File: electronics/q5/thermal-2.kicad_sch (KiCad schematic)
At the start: 5 parts, among them U5 Push-pull temperature window

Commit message: Q5 design lock: JLC Basic substitutions, re-verified board, cost estimator
Co-Authored-By: Claude Opus 5.5 <noreply@anthropic.com>
Claude-Session: https://claude.ai/code/session_01UrkzLMrBi6iLPSL5SbMCA7
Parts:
- R14, R15: MPN RC0603FR-07100KL -> 0603WAF1003T5E
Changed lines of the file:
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@@
       (in_bom yes) (on_board yes) (dnp no)
  (property "Reference" "R14" (at 294.64 73.66 0) (effects (font (size 1.524 1.524)))) (property "Value" "100k" (at 294.64 77.46999999999998 0) (effects (font (size 1.524 1.524))))
-      (property "Footprint" "CountFidgetQ5:Resistor_SMD_R_0603_1608Metric" (at 294.64 82.55 0) (effects (font (size 1.27 1.27)) (hide yes))) (property "MPN" "RC0603FR-07100KL" (at 294.64 77.46999999999998 0) (effects (font (size 1.524 1.524)) (hide yes)))
+      (property "Footprint" "CountFidgetQ5:Resistor_SMD_R_0603_1608Metric" (at 294.64 82.55 0) (effects (font (size 1.27 1.27)) (hide yes))) (property "MPN" "0603WAF1003T5E" (at 294.64 77.46999999999998 0) (effects (font (size 1.524 1.524)) (hide yes)))
       (property "Description" "Local upper charge-enable gate pulldown; keep connected close to Q3 gate" (at 294.64 82.55 0) (effects (font (size 1.27 1.27)) (hide yes)))
       (pin "1")(pin "2")
@@
       (in_bom yes) (on_board yes) (dnp no)
  (property "Reference" "R15" (at 105.41 152.4 0) (effects (font (size 1.524 1.524)))) (property "Value" "100k" (at 105.41 156.21 0) (effects (font (size 1.524 1.524))))
-      (property "Footprint" "CountFidgetQ5:Resistor_SMD_R_0603_1608Metric" (at 105.41 161.29 0) (effects (font (size 1.27 1.27)) (hide yes))) (property "MPN" "RC0603FR-07100KL" (at 105.41 156.21 0) (effects (font (size 1.524 1.524)) (hide yes)))
+      (property "Footprint" "CountFidgetQ5:Resistor_SMD_R_0603_1608Metric" (at 105.41 161.29 0) (effects (font (size 1.27 1.27)) (hide yes))) (property "MPN" "0603WAF1003T5E" (at 105.41 156.21 0) (effects (font (size 1.524 1.524)) (hide yes)))
       (property "Description" "Local lower charge-enable gate pulldown; keep connected close to Q4 gate" (at 105.41 161.29 0) (effects (font (size 1.27 1.27)) (hide yes)))
       (pin "1")(pin "2")

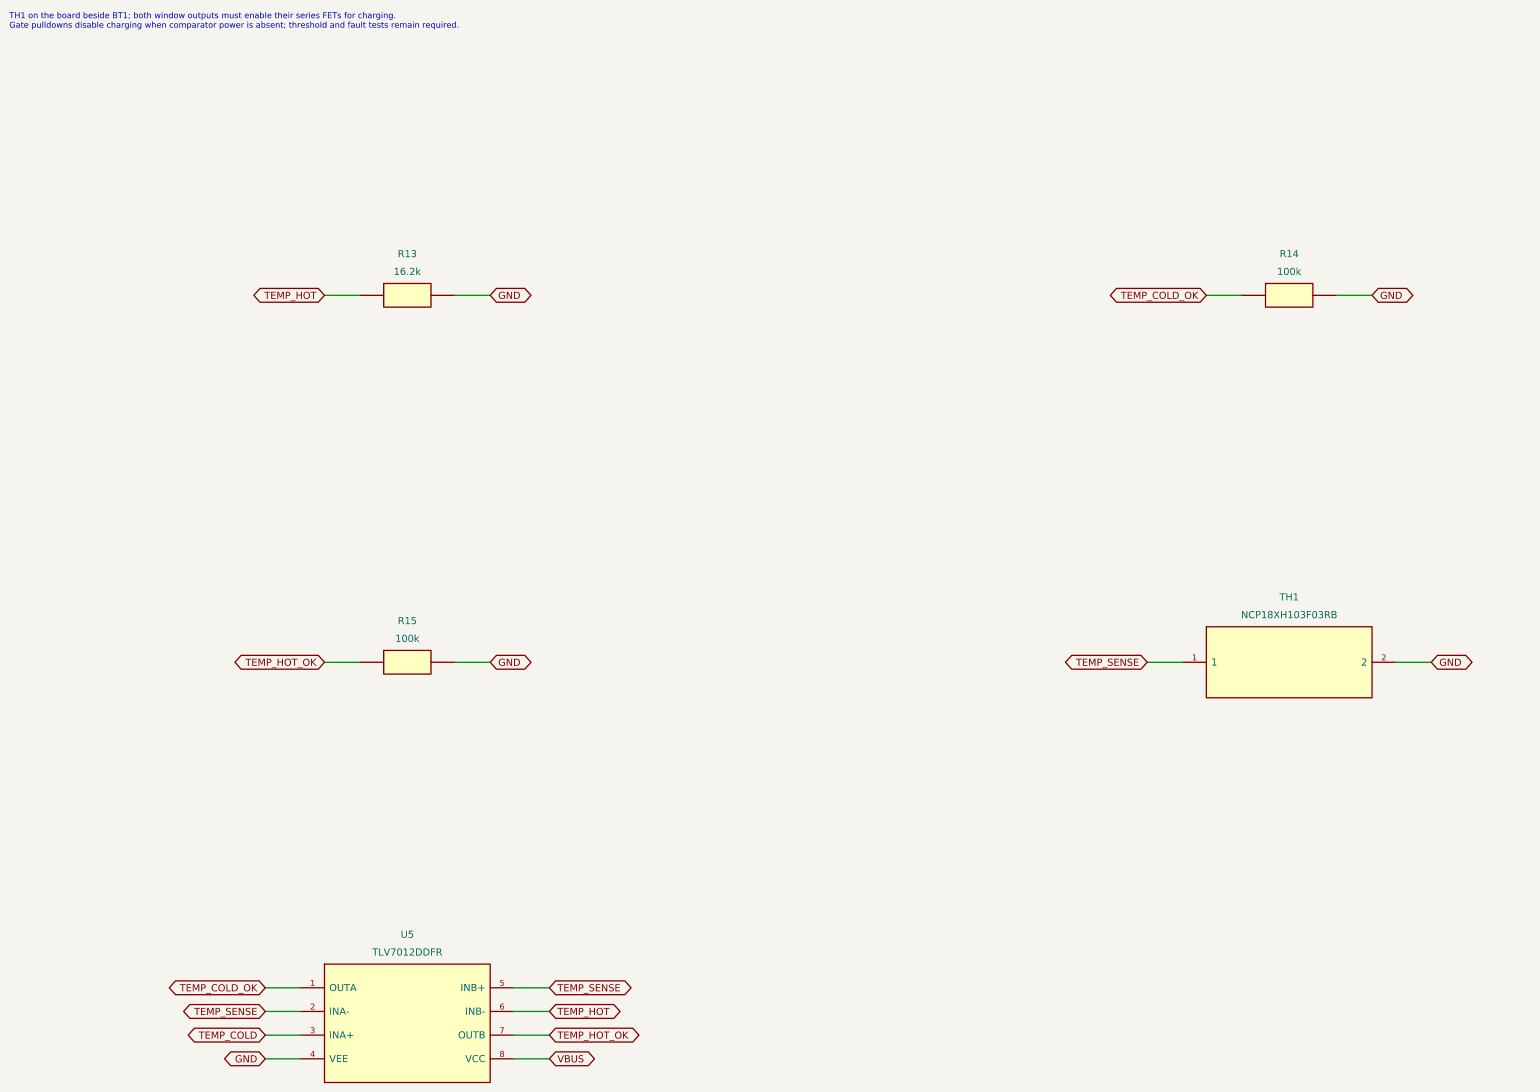
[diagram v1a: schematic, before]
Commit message: First-order de-risking: U5 supply filter, 10 nF latch cap, JLC-corrected CPLs, DFU unplug rule
Three independent checks (datasheet pinouts, JLC EasyEDA footprints, dead-on-arrival
review) found no pinout, footprint or DOA defect. Changes from their findings:
R39 1k + C9 filter U5's 6 V abs-max supply from VBUS hot-plug ringing; C40 10 nF
(min latch press 10.5 ms typ); JLC-corrected CPL files and a preview checklist;
flasher warns to reset a unit left in DFU before unplugging. Board re-routed:
DRC/ERC/parity zero, no via-to-land gaps; emulator 0 failures; stock 43/43.

Co-Authored-By: Claude Opus 5.5 <noreply@anthropic.com>
Claude-Session: https://claude.ai/code/session_01UrkzLMrBi6iLPSL5SbMCA7
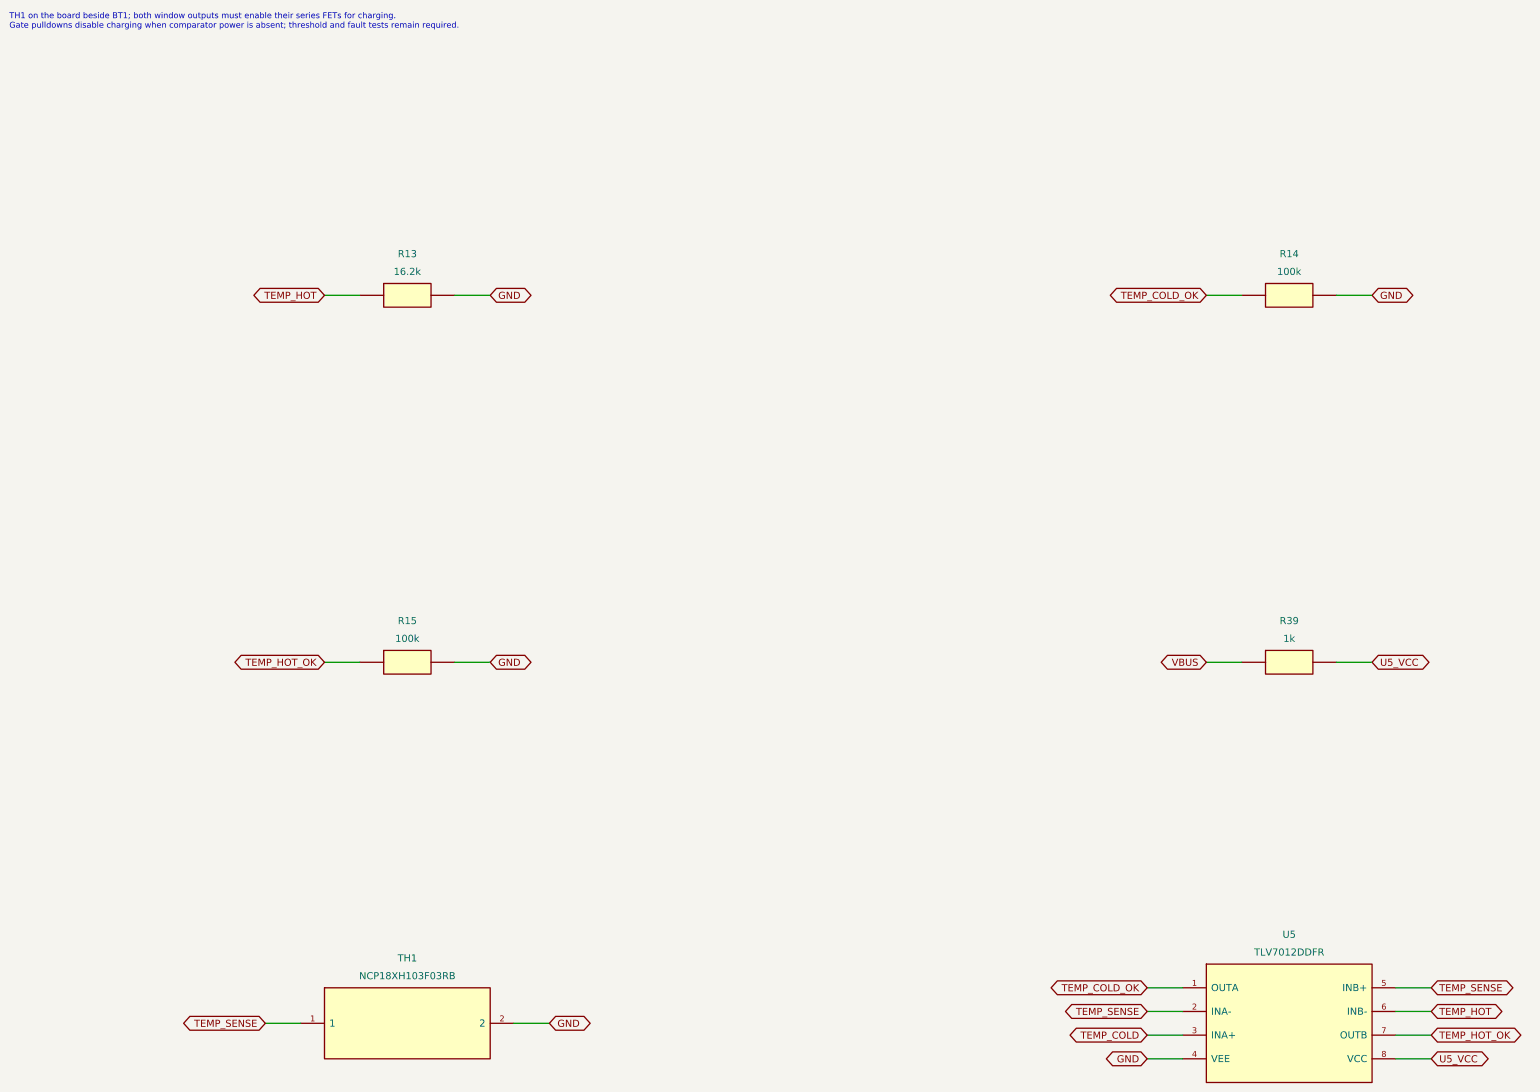
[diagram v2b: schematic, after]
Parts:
- added R39: 1k, CountFidgetQ5:Resistor_SMD_R_0603_1608Metric, symbol CountFidgetQ5:R39
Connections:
- net VBUS: now also R39.1; no longer U5.8 (VCC)
- new net U5_VCC: R39.2, U5.8 (VCC)
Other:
- moved on the sheet: TH1, U5

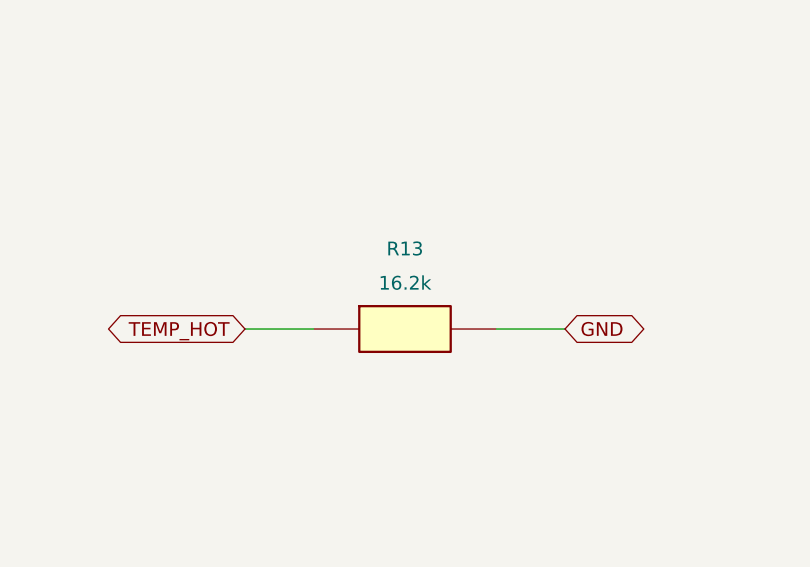
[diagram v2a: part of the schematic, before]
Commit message: Move nine part types to JLC Basic; 16 Extended types remain, each justified
R4 18k (16.7 mA charge), temperature window 56k/82k/18k/12k (7.26-35.83 C),
R32 75 ohm, Q1/Q2 AO3400A, 2.2 uF and 10 uF 50 V 0805 capacitors. Fresh
ERC/DRC/parity on unchanged routing, stock 42/42, exports, JLC footprint
fit and pin names, power/latch checks re-run. About $28 less per order.

Co-Authored-By: Claude Opus 5.5 <noreply@anthropic.com>
Claude-Session: https://claude.ai/code/session_01UrkzLMrBi6iLPSL5SbMCA7
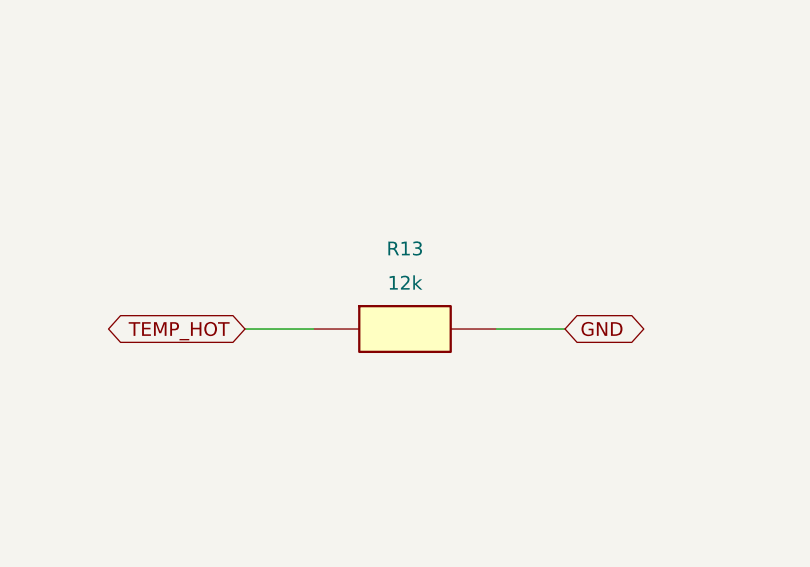
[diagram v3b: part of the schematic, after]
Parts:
- R13: value 16.2k -> 12k; MPN 0603WAF1622T5E -> 0603WAF1202T5E
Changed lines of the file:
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@@
 (symbol (lib_id "CountFidgetQ5:R13") (at 105.41 82.55 0) (unit 1) (exclude_from_sim no)
       (in_bom yes) (on_board yes) (dnp no)
- (property "Reference" "R13" (at 105.41 73.66 0) (effects (font (size 1.524 1.524)))) (property "Value" "16.2k" (at 105.41 77.46999999999998 0) (effects (font (size 1.524 1.524))))
-      (property "Footprint" "CountFidgetQ5:Resistor_SMD_R_0603_1608Metric" (at 105.41 82.55 0) (effects (font (size 1.27 1.27)) (hide yes))) (property "MPN" "0603WAF1622T5E" (at 105.41 77.46999999999998 0) (effects (font (size 1.524 1.524)) (hide yes)))
+ (property "Reference" "R13" (at 105.41 73.66 0) (effects (font (size 1.524 1.524)))) (property "Value" "12k" (at 105.41 77.46999999999998 0) (effects (font (size 1.524 1.524))))
+      (property "Footprint" "CountFidgetQ5:Resistor_SMD_R_0603_1608Metric" (at 105.41 82.55 0) (effects (font (size 1.27 1.27)) (hide yes))) (property "MPN" "0603WAF1202T5E" (at 105.41 77.46999999999998 0) (effects (font (size 1.524 1.524)) (hide yes)))
       (property "Description" "1%, 0603, 0.1 W" (at 105.41 82.55 0) (effects (font (size 1.27 1.27)) (hide yes)))
       (pin "1")(pin "2")
